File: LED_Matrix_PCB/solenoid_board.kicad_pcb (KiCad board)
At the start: 2 copper layers, 105 x 90 mm, 107 parts, among them J2 MCU_LEFT_LEGS, J3 MCU_RIGHT_LEGS

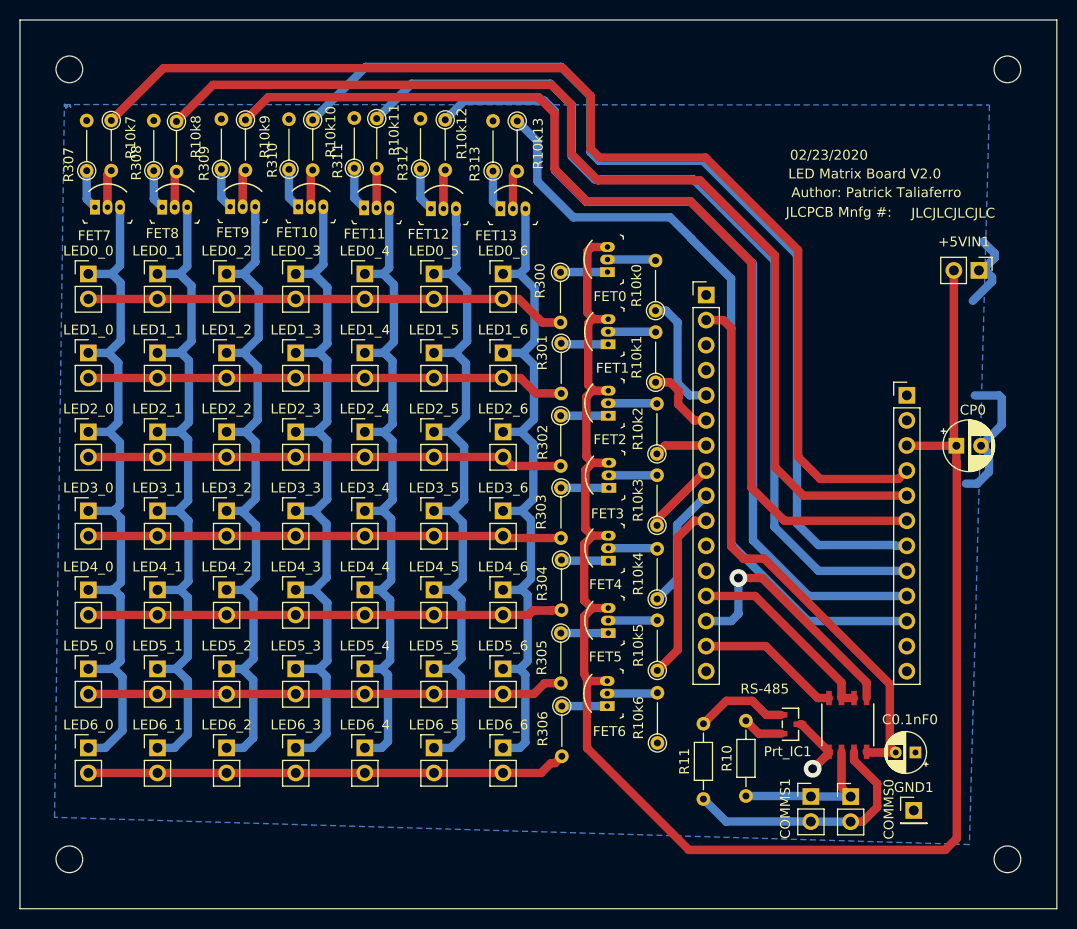
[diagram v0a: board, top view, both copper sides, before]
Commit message: Changed mosfet circuitry.
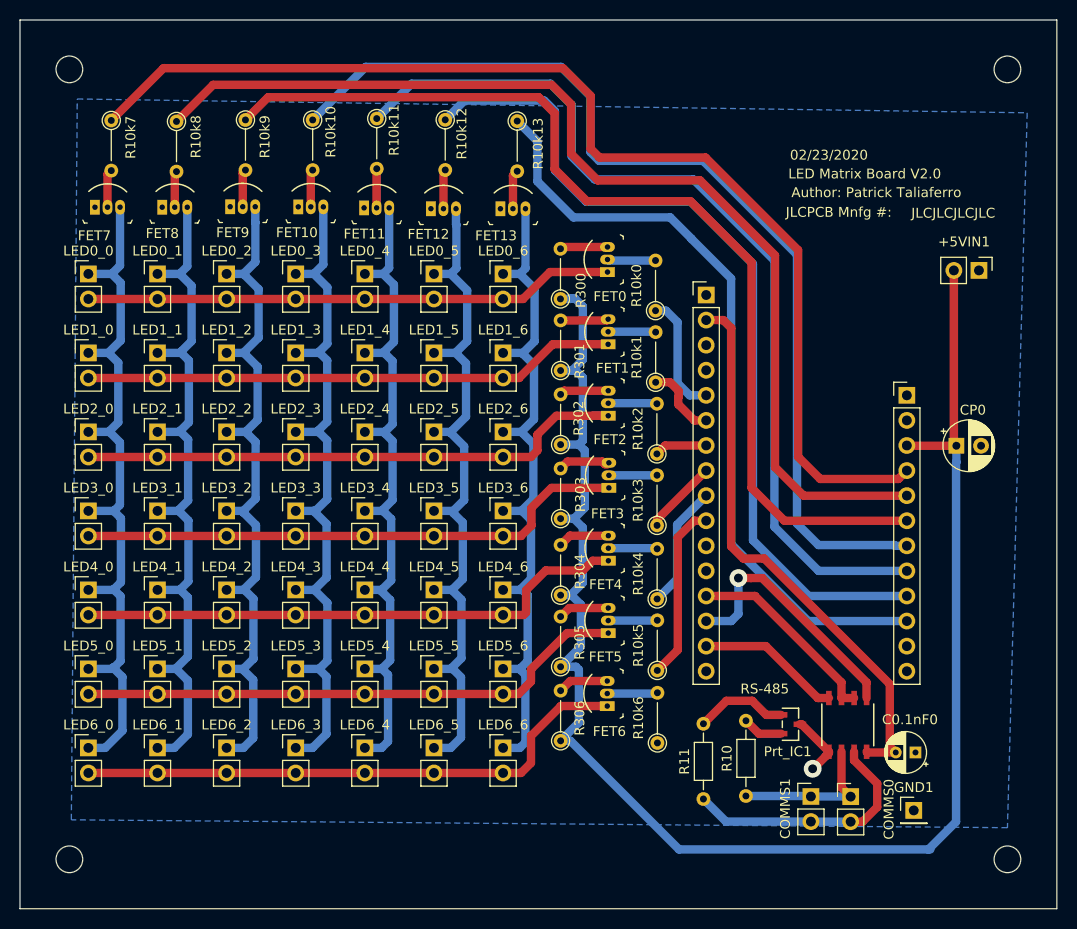
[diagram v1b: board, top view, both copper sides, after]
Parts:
- removed R307, R308, R309, R310, R311, R312, R313: 300, Resistor_THT:R_Axial_DIN0204_L3.6mm_D1.6mm_P5.08mm_Vertical
- moved R304 3.56 mm to (169.8, 108.2), turned to 90 degrees
- moved R306 3.52 mm to (169.8, 123.0), turned to 90 degrees
- moved R305 3.41 mm to (169.8, 115.5), turned to 90 degrees
- moved R303 3.12 mm to (169.8, 100.5), turned to 90 degrees
- moved R302 2.92 mm to (169.8, 93.0), turned to 90 degrees
- moved R301 2.76 mm to (169.8, 85.5), turned to 90 degrees
- moved R300 2.70 mm to (169.7, 78.2), turned to 90 degrees
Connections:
- FET0 pad 1: Net-(FET0-Pad1) -> /ROW0
- FET0 pad 3: +5V -> Net-(FET0-Pad3)
- FET1 pad 1: Net-(FET1-Pad1) -> /ROW1
- FET1 pad 3: +5V -> Net-(FET1-Pad3)
- FET10 pad 1: Net-(FET10-Pad1) -> GND
- FET11 pad 1: Net-(FET11-Pad1) -> GND
- FET12 pad 1: Net-(FET12-Pad1) -> GND
- FET13 pad 1: Net-(FET13-Pad1) -> GND
- FET2 pad 1: Net-(FET2-Pad1) -> /ROW2
- FET2 pad 3: +5V -> Net-(FET2-Pad3)
- FET3 pad 1: Net-(FET3-Pad1) -> /ROW3
- FET3 pad 3: +5V -> Net-(FET3-Pad3)
- FET4 pad 1: Net-(FET4-Pad1) -> /ROW4
- FET4 pad 3: +5V -> Net-(FET4-Pad3)
- FET5 pad 1: Net-(FET5-Pad1) -> /ROW5
- FET5 pad 3: +5V -> Net-(FET5-Pad3)
- FET6 pad 1: Net-(FET6-Pad1) -> /ROW6
- FET6 pad 3: +5V -> Net-(FET6-Pad3)
- FET7 pad 1: Net-(FET7-Pad1) -> GND
- FET8 pad 1: Net-(FET8-Pad1) -> GND
- FET9 pad 1: Net-(FET9-Pad1) -> GND
- J2 pad 7: /A2 -> (no net)
- R10k2 pad 1: /A2 -> (no net)
- R300 pad 1: Net-(FET0-Pad1) -> +5V
- R300 pad 2: /ROW0 -> Net-(FET0-Pad3)
- R301 pad 1: Net-(FET1-Pad1) -> +5V
- R301 pad 2: /ROW1 -> Net-(FET1-Pad3)
- R302 pad 1: Net-(FET2-Pad1) -> +5V
- R302 pad 2: /ROW2 -> Net-(FET2-Pad3)
- R303 pad 1: Net-(FET3-Pad1) -> +5V
- R303 pad 2: /ROW3 -> Net-(FET3-Pad3)
- R304 pad 1: Net-(FET4-Pad1) -> +5V
- R304 pad 2: /ROW4 -> Net-(FET4-Pad3)
- R305 pad 1: Net-(FET5-Pad1) -> +5V
- R305 pad 2: /ROW5 -> Net-(FET5-Pad3)
- R306 pad 1: Net-(FET6-Pad1) -> +5V
- R306 pad 2: /ROW6 -> Net-(FET6-Pad3)
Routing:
- net GND: track 29.9 -> 6.49 mm
- net /ROW2: track 48.2 -> 56.9 mm
- net /ROW6: track 48.7 -> 57.0 mm
- net /ROW4: track 48.1 -> 56.3 mm
- net /ROW3: track 47.9 -> 55.8 mm
- net /ROW5: track 48.3 -> 55.9 mm
- net /ROW1: track 48.5 -> 54.4 mm
- net Net-(FET3-Pad3): track 0.00 -> 5.35 mm
- net /A2: track 5.34 -> 0.00 mm
- net (no net): track 0.00 -> 5.34 mm
- net Net-(FET4-Pad3): track 0.00 -> 5.23 mm
- net Net-(FET5-Pad3): track 0.00 -> 5.18 mm
- net Net-(FET6-Pad3): track 0.00 -> 5.13 mm
- net Net-(FET2-Pad3): track 0.00 -> 4.98 mm
- net /ROW0: track 48.8 -> 53.7 mm
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
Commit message: Added a pull down resistor and re-routed. Also, updated BOM.
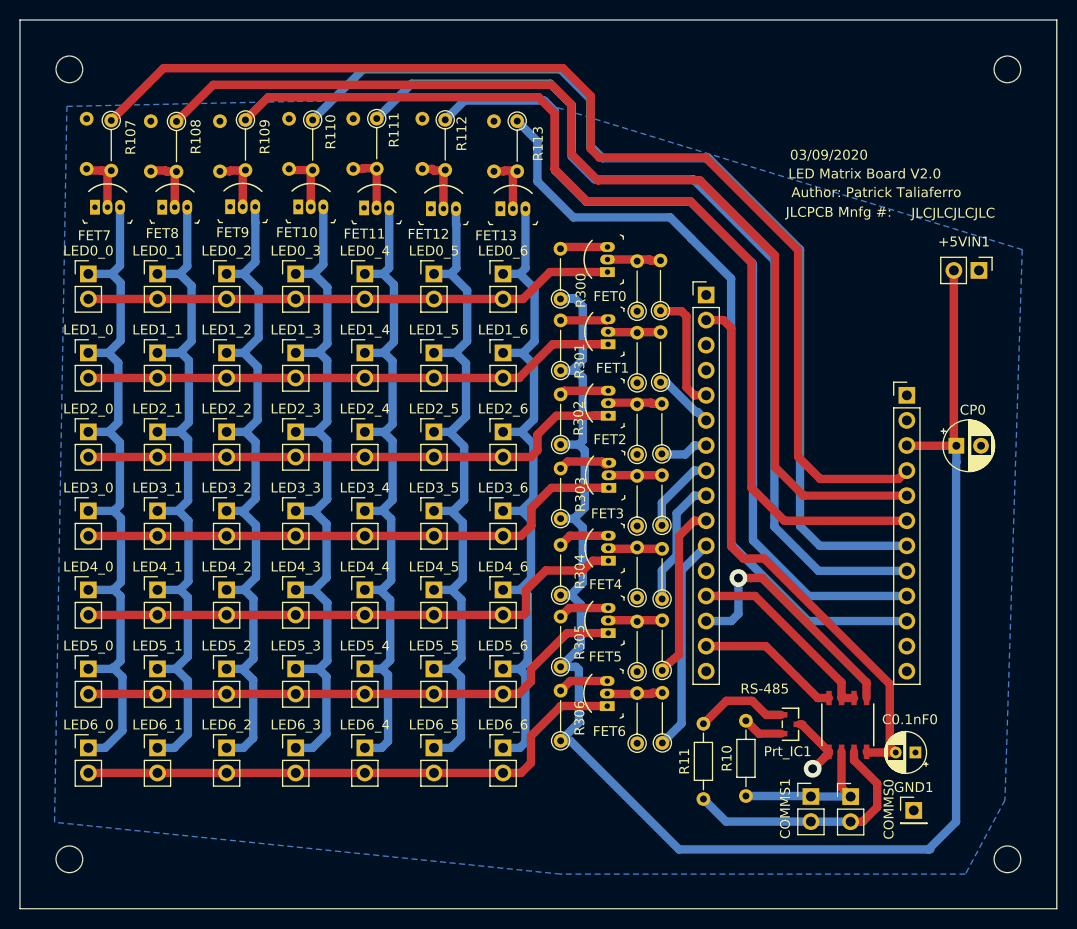
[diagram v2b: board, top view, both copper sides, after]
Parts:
- added R3k0: 3k, Resistor_THT:R_Axial_DIN0204_L3.6mm_D1.6mm_P5.08mm_Vertical, F.Cu at (177.5, 79.5)
- added R3k1: 3k, Resistor_THT:R_Axial_DIN0204_L3.6mm_D1.6mm_P5.08mm_Vertical, F.Cu at (177.5, 86.8)
- added R3k10: 3k, Resistor_THT:R_Axial_DIN0204_L3.6mm_D1.6mm_P5.08mm_Vertical, B.Cu at (142.2, 60.0)
- added R3k11: 3k, Resistor_THT:R_Axial_DIN0204_L3.6mm_D1.6mm_P5.08mm_Vertical, B.Cu at (148.8, 60.0)
- added R3k12: 3k, Resistor_THT:R_Axial_DIN0204_L3.6mm_D1.6mm_P5.08mm_Vertical, B.Cu at (155.8, 60.0)
- added R3k13: 3k, Resistor_THT:R_Axial_DIN0204_L3.6mm_D1.6mm_P5.08mm_Vertical, B.Cu at (163.0, 60.2)
- added R3k2: 3k, Resistor_THT:R_Axial_DIN0204_L3.6mm_D1.6mm_P5.08mm_Vertical, F.Cu at (177.5, 94.0)
- added R3k3: 3k, Resistor_THT:R_Axial_DIN0204_L3.6mm_D1.6mm_P5.08mm_Vertical, F.Cu at (177.5, 101.2)
- added R3k4: 3k, Resistor_THT:R_Axial_DIN0204_L3.6mm_D1.6mm_P5.08mm_Vertical, F.Cu at (177.5, 108.5)
- added R3k5: 3k, Resistor_THT:R_Axial_DIN0204_L3.6mm_D1.6mm_P5.08mm_Vertical, F.Cu at (177.5, 116.0)
- added R3k6: 3k, Resistor_THT:R_Axial_DIN0204_L3.6mm_D1.6mm_P5.08mm_Vertical, F.Cu at (177.5, 123.2)
- added R3k7: 3k, Resistor_THT:R_Axial_DIN0204_L3.6mm_D1.6mm_P5.08mm_Vertical, B.Cu at (121.8, 60.0)
- added R3k8: 3k, Resistor_THT:R_Axial_DIN0204_L3.6mm_D1.6mm_P5.08mm_Vertical, B.Cu at (128.2, 60.2)
- added R3k9: 3k, Resistor_THT:R_Axial_DIN0204_L3.6mm_D1.6mm_P5.08mm_Vertical, B.Cu at (135.2, 60.2)
- R100: renamed from R10k0; value 10k -> 100
- R101: renamed from R10k1; value 10k -> 10
- R102: renamed from R10k2; value 10k -> 100
- R103: renamed from R10k3; value 10k -> 100
- R104: renamed from R10k4; value 10k -> 100
- R105: renamed from R10k5; value 10k -> 100
- R106: renamed from R10k6; value 10k -> 100
- R107: renamed from R10k7; value 10k -> 100
- R108: renamed from R10k8; value 10k -> 100
- R109: renamed from R10k9; value 10k -> 100
- R110: renamed from R10k10; value 10k -> 100
- R111: renamed from R10k11; value 10k -> 100
- R112: renamed from R10k12; value 10k -> 100
- R113: renamed from R10k13; value 10k -> 100
- moved R100 0.50 mm to (179.9, 79.4)
- moved R101 0.50 mm to (179.9, 86.7)
- moved R102 0.50 mm to (180.0, 93.9)
- moved R103 0.50 mm to (180.0, 101.2)
- moved R104 0.50 mm to (180.0, 108.6)
- moved R105 0.50 mm to (180.0, 115.9)
- moved R106 0.50 mm to (180.1, 123.2)
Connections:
- J2 pad 1: (no net) -> /RST
- J2 pad 11: (no net) -> /SCK
- J2 pad 12: (no net) -> /MOSI
- J2 pad 3: (no net) -> /ARf
- J2 pad 7: (no net) -> /A2
- J3 pad 1: (no net) -> /BAT
- J3 pad 11: (no net) -> /SCL
- J3 pad 12: (no net) -> /SDA
- J3 pad 2: (no net) -> /En
- R102 pad 1: (no net) -> /A2
- R106 pad 1: (no net) -> /SCK
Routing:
- net /SCK: track 0.00 -> 22.1 mm
- net (no net): track 5.34 -> 0.00 mm
- net /A2: track 0.00 -> 4.87 mm
- net Net-(FET12-Pad2): track 4.00 -> 6.82 mm
- net Net-(FET10-Pad2): track 3.80 -> 6.46 mm
- net Net-(FET8-Pad2): track 3.68 -> 6.32 mm
- net Net-(FET13-Pad2): track 3.98 -> 6.51 mm
- net Net-(FET9-Pad2): track 3.82 -> 6.36 mm
- net Net-(FET11-Pad2): track 3.97 -> 6.50 mm
- net Net-(FET7-Pad2): track 3.87 -> 6.36 mm
- net /A1: track 7.57 -> 6.32 mm
- net Net-(FET4-Pad2): track 4.97 -> 5.80 mm
- net /A4: track 12.5 -> 13.1 mm
- net Net-(FET2-Pad2): track 4.95 -> 5.55 mm
- net Net-(FET1-Pad2): track 4.83 -> 5.42 mm
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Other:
- board text added: "03/09/2020"
- board text removed: "02/23/2020"
